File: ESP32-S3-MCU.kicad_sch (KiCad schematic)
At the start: 44 parts, among them SW1 RESET, SW2 BOOT, X1 32.768KHz

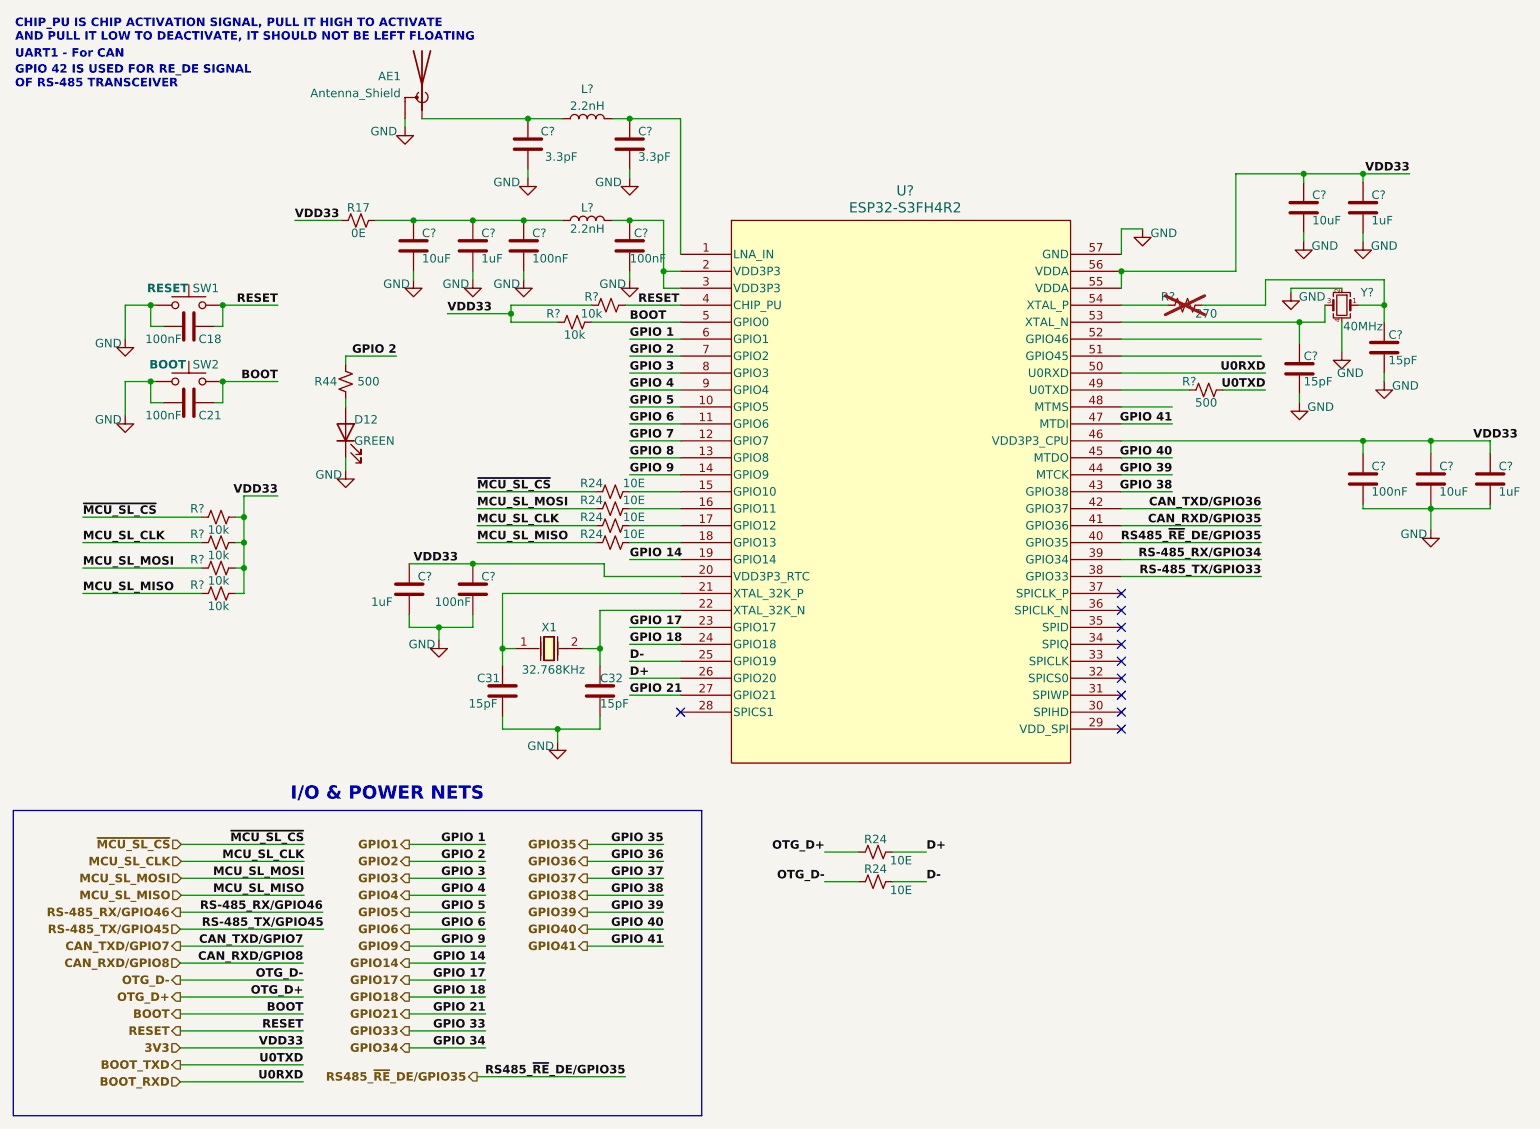
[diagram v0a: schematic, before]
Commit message: Changed MCU pin mapping
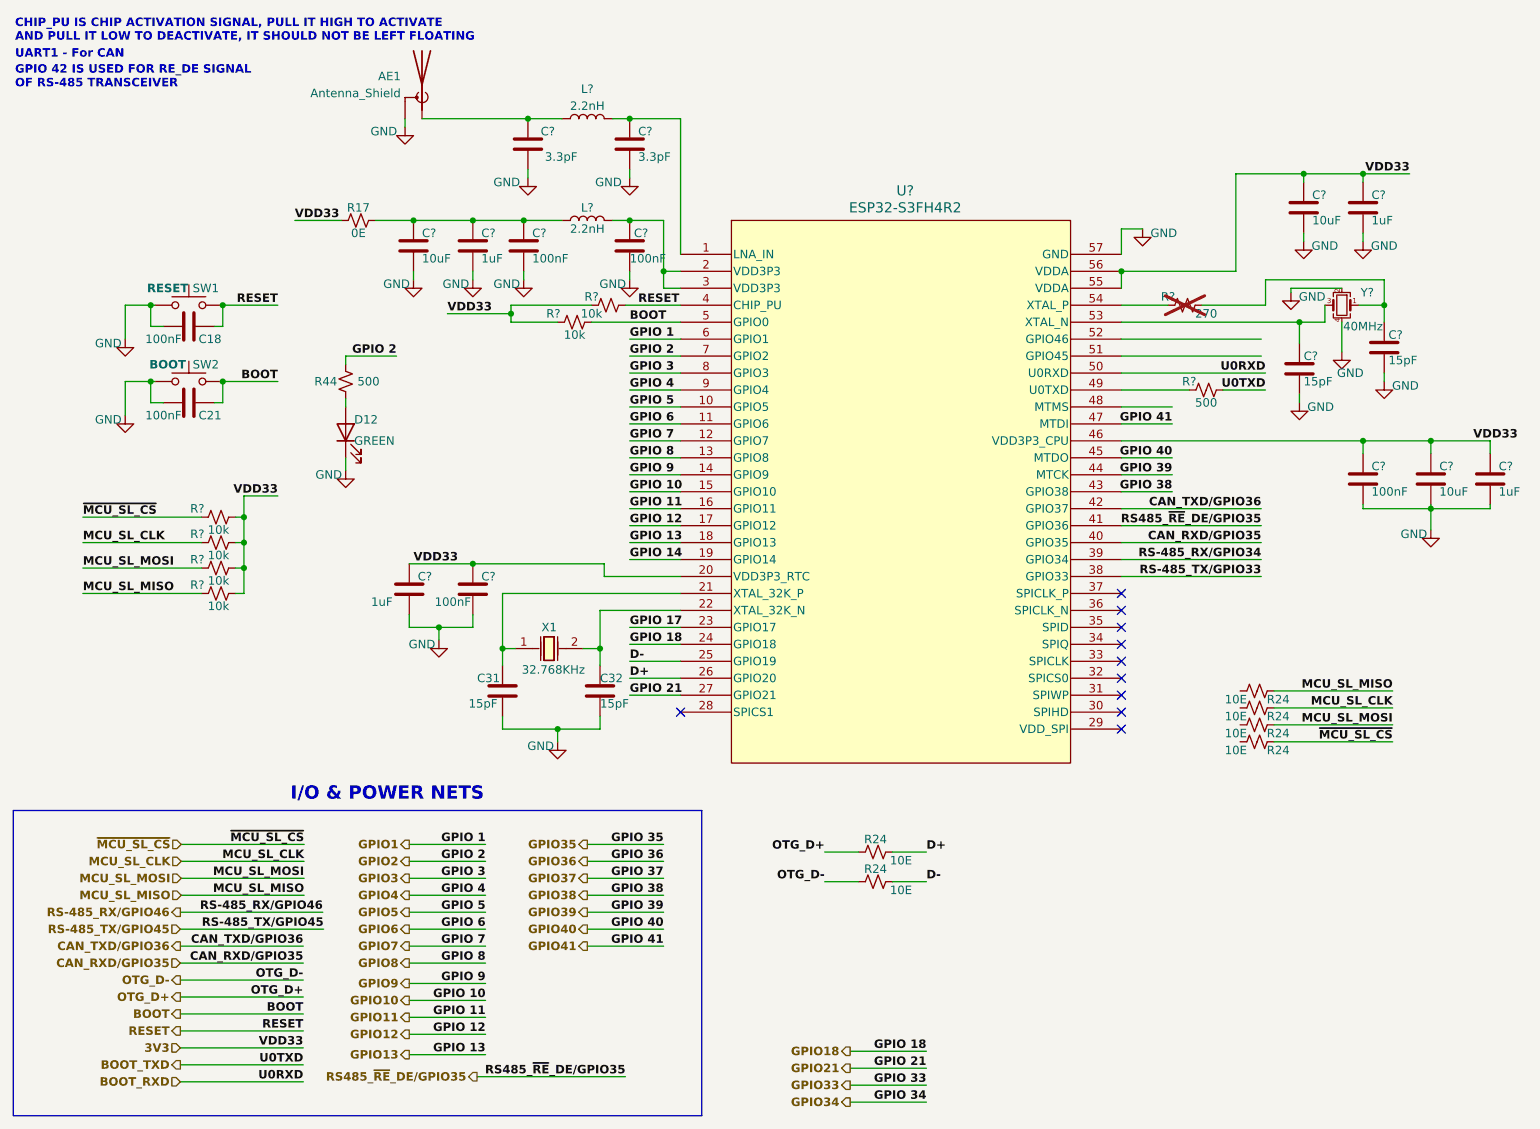
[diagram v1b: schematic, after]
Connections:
- net CAN_RXD/GPIO35: now also U?.40 (GPIO35); no longer U?.41 (GPIO36)
- net RS485_~{RE}_DE/GPIO35: now also U?.41 (GPIO36); no longer U?.40 (GPIO35)
- net at R24.2: no longer U?.17 (GPIO12)
- net at R24.2: no longer U?.16 (GPIO11)
- net at R24.2: no longer U?.15 (GPIO10)
- net at R24.2: no longer U?.18 (GPIO13)
- net GPIO 7 renamed GPIO7
- net GPIO 8 renamed GPIO8
- net GPIO14 renamed GPIO 14
- net GPIO17 renamed GPIO 17
- new net GPIO10: U?.15 (GPIO10)
- new net GPIO11: U?.16 (GPIO11)
- new net GPIO12: U?.17 (GPIO12)
- new net GPIO13: U?.18 (GPIO13)
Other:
- moved on the sheet: R24

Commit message: Completed routing for all GPIO pins
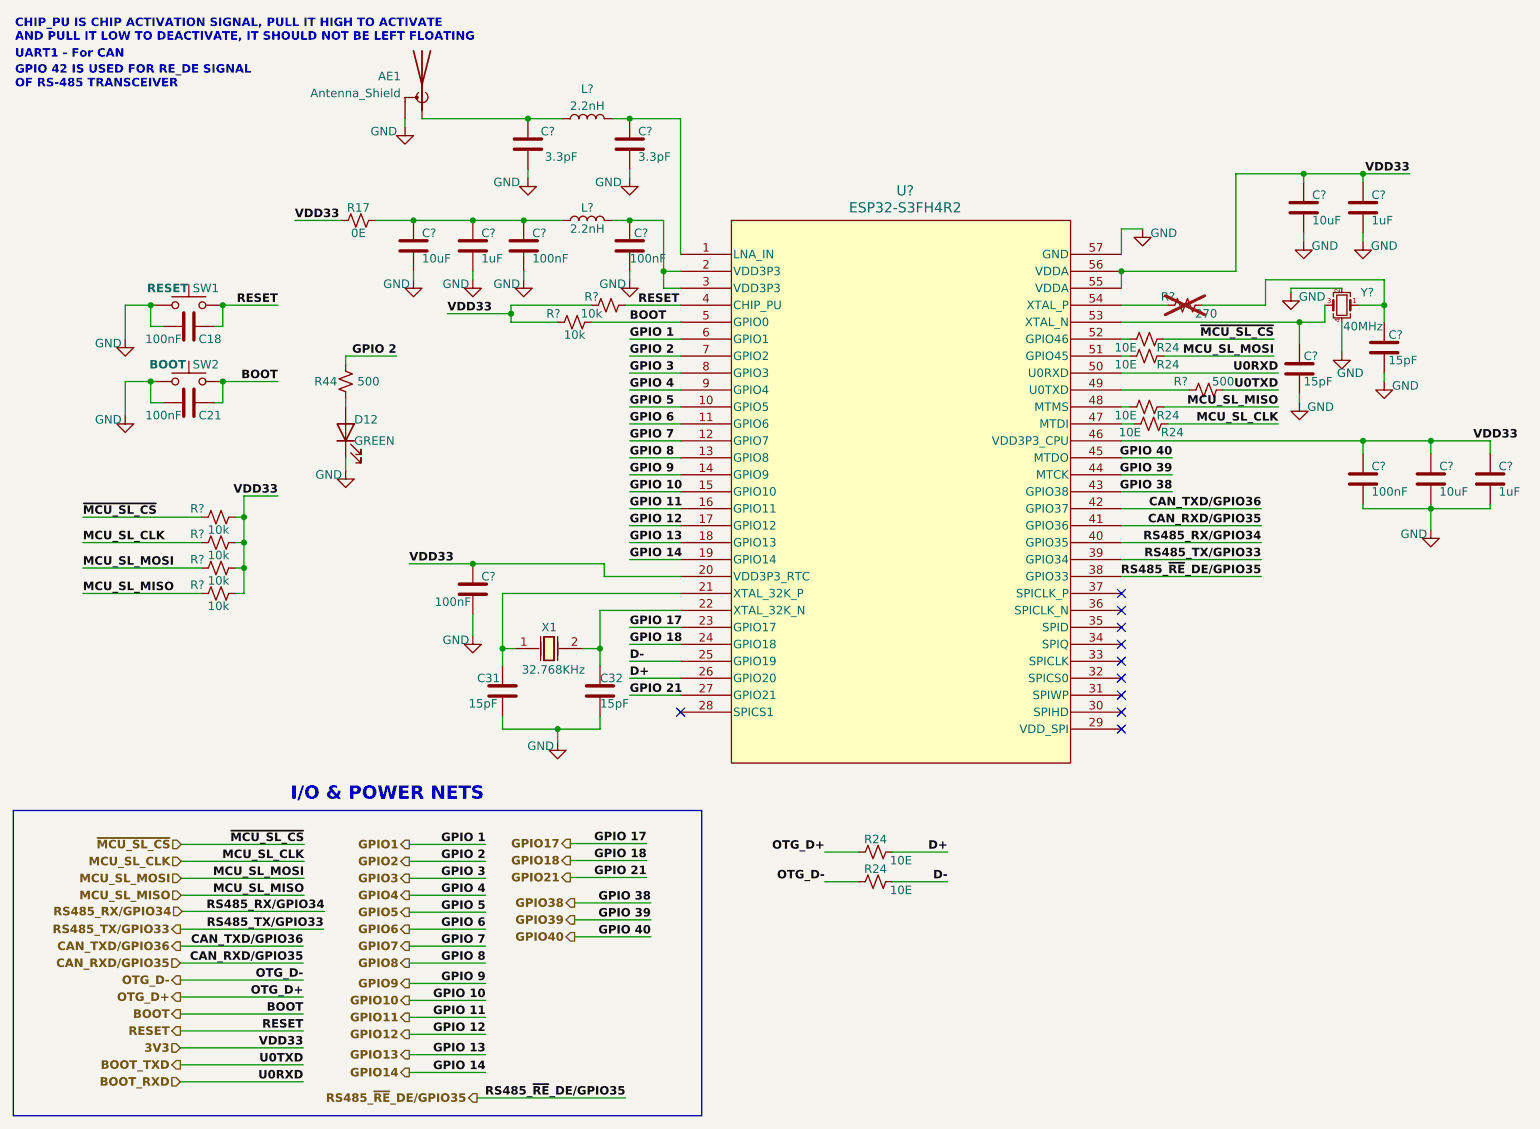
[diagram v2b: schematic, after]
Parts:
- removed C?: 1uF, ESP32-S3_Dev_Board:C_0603_1608Metric, symbol ESP32-S3_DB:C
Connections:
- net GPIO41 is gone; now on an unnamed net: U?.47 (MTDI)
- net RS-485_TX/GPIO33 is gone; now on net RS485_~{RE}_DE/GPIO35: U?.38 (GPIO33)
- net CAN_RXD/GPIO35: now also U?.41 (GPIO36); no longer U?.40 (GPIO35)
- net MCU_SL_CLK: now also R24.1; no longer R24.1
- net MCU_SL_MISO: now also R24.1; no longer R24.1
- net MCU_SL_MOSI: now also R24.1; no longer R24.1
- net RS485_~{RE}_DE/GPIO35: no longer U?.41 (GPIO36)
- net ~{MCU_SL_CS}: now also R24.1; no longer R24.1
- net at R24.2: now also U?.51 (GPIO45)
- net at R24.2: now also U?.48 (MTMS)
- net at U?.52 (GPIO46): now also R24.2
- net GPIO 14 renamed GPIO14
- net GPIO 17 renamed GPIO17
- net RS-485_RX/GPIO34 renamed RS485_TX/GPIO33
- new net RS485_RX/GPIO34: U?.40 (GPIO35)
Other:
- moved on the sheet: R24

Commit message: Merge changes upstream
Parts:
- removed C?: 10uF, ESP32-S3_Dev_Board:C_0805_2012Metric, symbol ESP32-S3_DB:C
- removed C?: 1uF, ESP32-S3_Dev_Board:C_0603_1608Metric, symbol ESP32-S3_DB:C
- removed R?: 500, ESP32-S3_Dev_Board:R_0402_1005Metric, symbol ESP32-S3_DB:R_Small_US
- R?: now fitted; now in the parts list
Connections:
- net GPIO10 is gone; now on an unnamed net: U?.15 (GPIO10)
- net GPIO11 is gone; now on an unnamed net: U?.16 (GPIO11)
- net GPIO12 is gone; now on an unnamed net: U?.17 (GPIO12)
- net GPIO13 is gone; now on an unnamed net: U?.18 (GPIO13)
- net GPIO7 is gone; now on net BOOT_TXD: U?.12 (GPIO7)
- net GPIO8 is gone; now on net BOOT_RXD: U?.13 (GPIO8)
- net BOOT_RXD: no longer U?.50 (U0RXD)
- net GPIO9: now also U?.48 (MTMS); no longer U?.14 (GPIO9)
- net MCU_SL_CLK: now also R24.1; no longer R24.1
- net MCU_SL_MISO: now also R24.1; no longer R24.1
- net MCU_SL_MOSI: now also R24.1; no longer R24.1
- net ~{MCU_SL_CS}: now also R24.1; no longer R24.1
- net at R24.2: no longer U?.51 (GPIO45)
- net at R24.2: no longer U?.48 (MTMS)
- net XTALP: now reaches C31.1, U?.21 (XTAL_32K_P), X1.1
- net XTALN: now reaches C32.1, U?.22 (XTAL_32K_N), X1.2
- net CAN_TXD/GPIO7: now reaches U?.49 (U0TXD)
- net at R24.2: no longer U?.47 (MTDI)
- net at R24.2: no longer U?.52 (GPIO46)
- net CAN_RXD/GPIO35 renamed GPIO36
- net CAN_TXD/GPIO36 renamed GPIO37
- net RS485_RX/GPIO34 renamed GPIO35
- net RS485_TX/GPIO33 renamed GPIO34
- net RS485_~{RE}_DE/GPIO35 renamed GPIO33
- new net CAN_RXD/GPIO8: U?.50 (U0RXD)
- new net GPIO41: U?.47 (MTDI)
- new net R4_~{RE}_DE: U?.14 (GPIO9)
- new net RS-485_RX/GPIO46: U?.52 (GPIO46)
- new net RS-485_TX/GPIO45: U?.51 (GPIO45)
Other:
- moved on the sheet: C?, R24

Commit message: Finished routing
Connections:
- net RS-485_RX/GPIO46 is gone; now on an unnamed net: U?.52 (GPIO46)
- net CAN_RXD/GPIO8: now also U?.48 (MTMS); no longer U?.50 (U0RXD)
- net CAN_TXD/GPIO7: now also U?.47 (MTDI); no longer U?.49 (U0TXD)
- net GPIO41: now also U?.18 (GPIO13); no longer U?.47 (MTDI)
- net GPIO9: now also U?.17 (GPIO12); no longer U?.48 (MTMS)
- net MCU_SL_CLK: now also R24.2; no longer R24.1
- net MCU_SL_MISO: now also R24.1, R?.1; no longer R24.1, R?.1
- net MCU_SL_MOSI: now also R24.2, R?.1; no longer R24.1, R?.1
- net at R24.2: now also U?.49 (U0TXD); no longer U?.16 (GPIO11)
- net at R24.2: no longer U?.15 (GPIO10)
- net GPIO33 renamed RS-485_TX/GPIO33
- net GPIO34 renamed RS-485_RX/GPIO34
- net RS-485_TX/GPIO45: no longer names the net of U?.51 (GPIO45)
- net RS-485_TX/GPIO45: now also R24.1
- new net: R24.1, U?.50 (U0RXD)
- new net GPIO45: U?.16 (GPIO11)
- new net GPIO46: U?.15 (GPIO10)
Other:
- moved on the sheet: C?, R24, R?, Y?
